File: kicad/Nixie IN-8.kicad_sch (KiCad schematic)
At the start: 47 parts, among them J1 HOURS, J10 DOT, J2 MINUTES, J3 DOT, J4 Conn_01x03_Pin, J5 Conn_01x03_Pin, J6 Conn_01x02_Pin, J7 Barrel_Jack_Switch, J8 HOURS, J9 MINUTES, Q1 MPSA42, SW1 SW_SPST, SW2 SW_SPST, SW3 SW_SPST, U1 K155ID1, U2 K155ID1, U3 K155ID1, U4 K155ID1, U5 MCP7940N-xP, U6 74HC595, U7 74HC595, Y1 32.768kHz

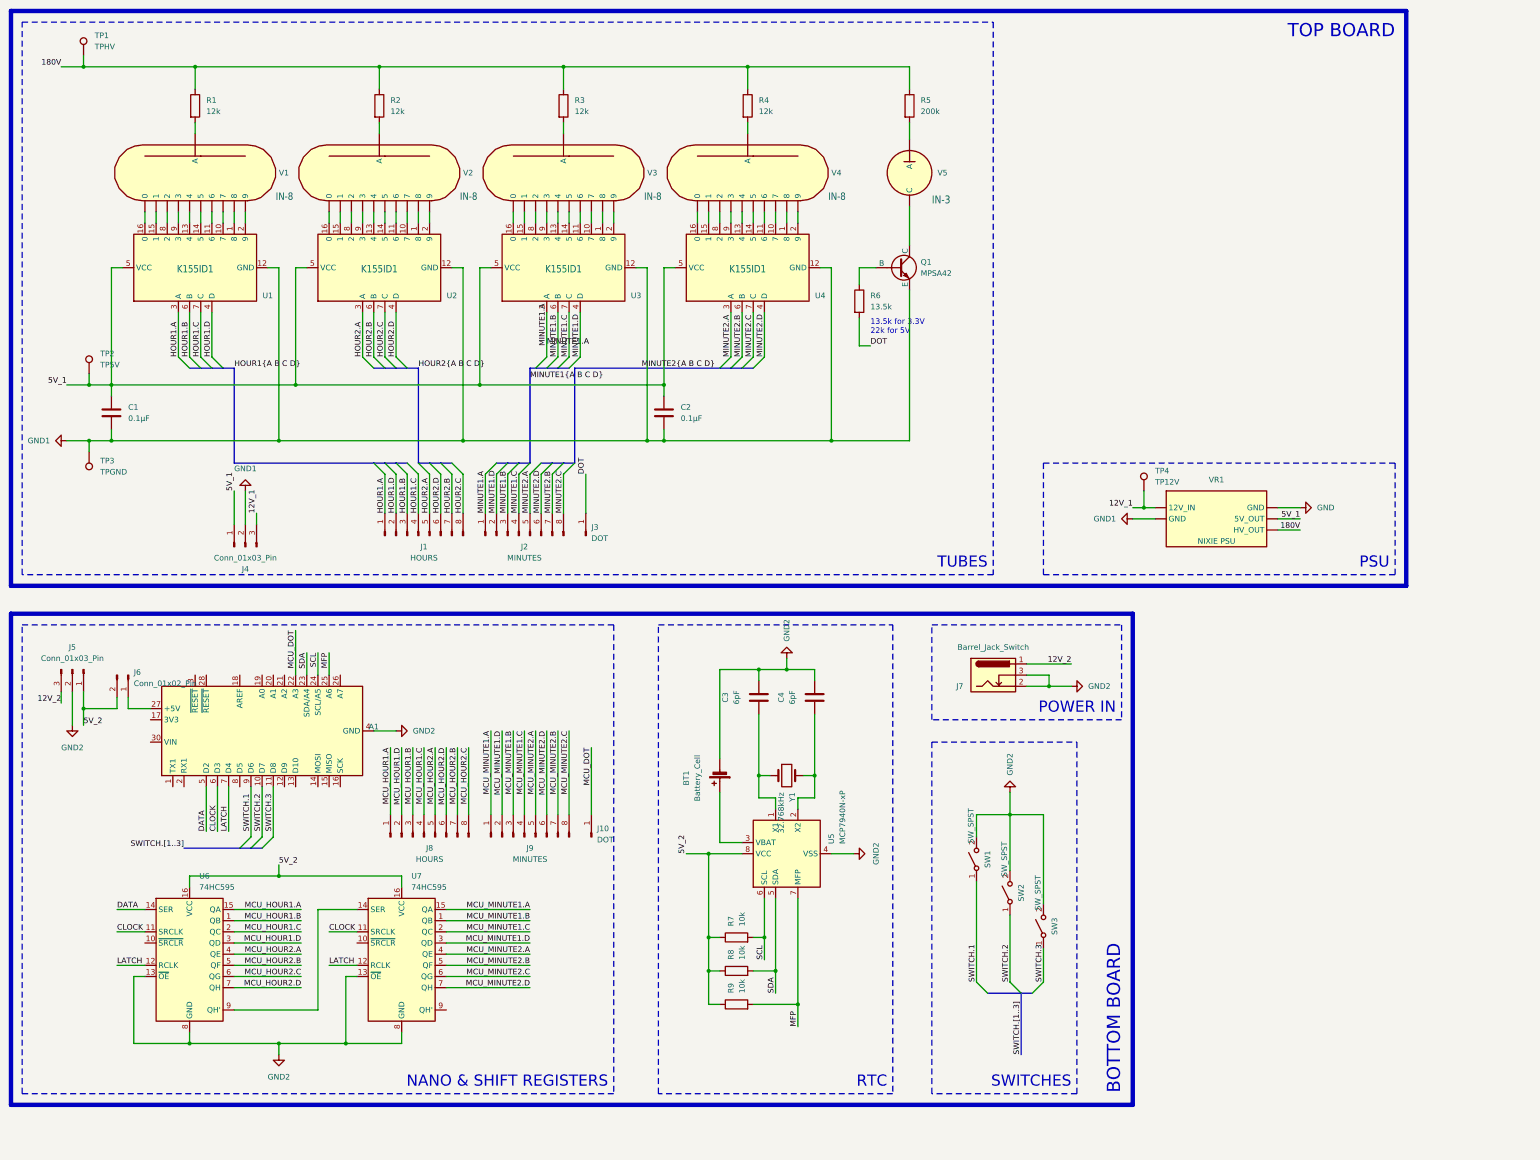
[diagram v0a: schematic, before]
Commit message: removed backups
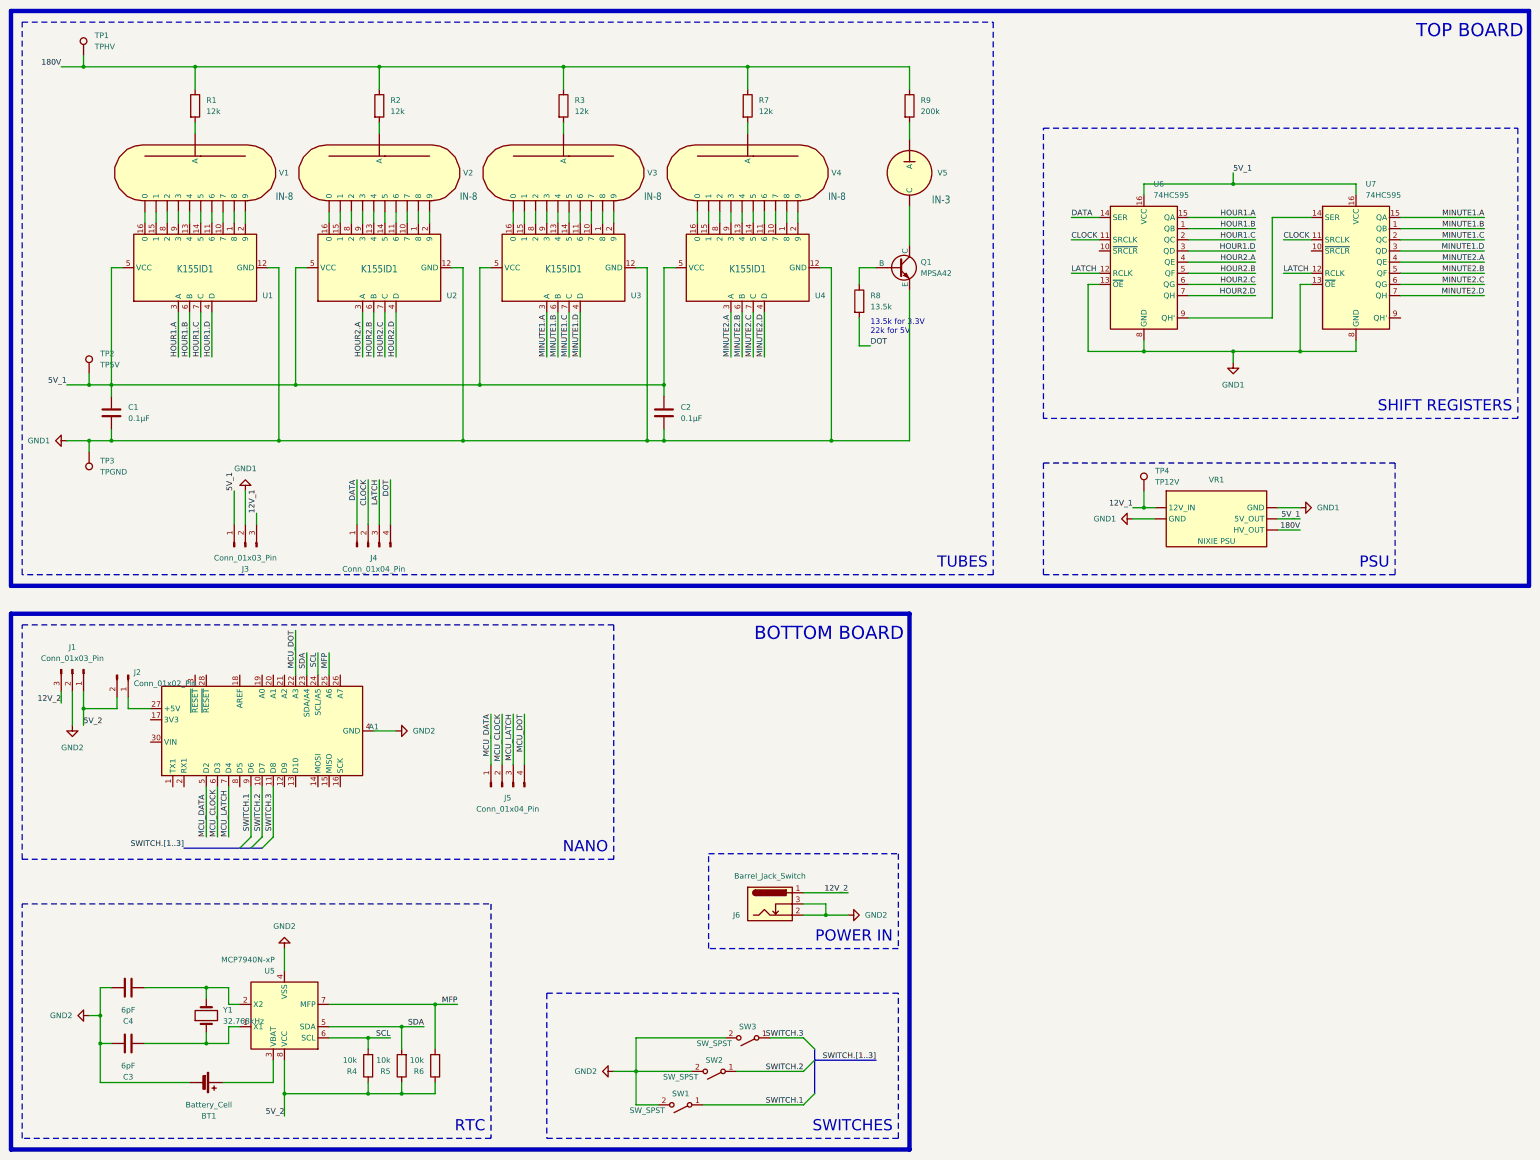
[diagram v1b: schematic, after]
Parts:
- removed J1, J8: HOURS, Connector_PinHeader_2.54mm:PinHeader_1x08_P2.54mm_Vertical, symbol Connector:Conn_01x08_Pin
- removed J10, J3: DOT, Connector_PinHeader_2.54mm:PinHeader_1x01_P2.54mm_Vertical, symbol Connector:Conn_01x01_Pin
- removed J2, J9: MINUTES, Connector_PinHeader_2.54mm:PinHeader_1x08_P2.54mm_Vertical, symbol Connector:Conn_01x08_Pin
- added J4, J5: Conn_01x04_Pin, Connector_PinHeader_2.54mm:PinHeader_1x04_P2.54mm_Vertical, symbol Connector:Conn_01x04_Pin
- renumbered J5 to J1, J6 to J2, J4 to J3, J7 to J6, R7 to R4, R8 to R5, R9 to R6, R4 to R7, R6 to R8, R5 to R9
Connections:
- net GND is gone; now on net GND1: VR1.4 (GND)
- net MCU_HOUR1.A is gone; now on net HOUR1.A: U6.15 (QA)
- net MCU_HOUR1.B is gone; now on net HOUR1.B: U6.1 (QB)
- net MCU_HOUR1.C is gone; now on net HOUR1.C: U6.2 (QC)
- net MCU_HOUR1.D is gone; now on net HOUR1.D: U6.3 (QD)
- net MCU_HOUR2.A is gone; now on net HOUR2.A: U6.4 (QE)
- net MCU_HOUR2.B is gone; now on net HOUR2.B: U6.5 (QF)
- net MCU_HOUR2.C is gone; now on net HOUR2.C: U6.6 (QG)
- net MCU_HOUR2.D is gone; now on net HOUR2.D: U6.7 (QH)
- net MCU_MINUTE1.A is gone; now on net MINUTE1.A: U7.15 (QA)
- net MCU_MINUTE1.B is gone; now on net MINUTE1.B: U7.1 (QB)
- net MCU_MINUTE1.C is gone; now on net MINUTE1.C: U7.2 (QC)
- net MCU_MINUTE1.D is gone; now on net MINUTE1.D: U7.3 (QD)
- net MCU_MINUTE2.A is gone; now on net MINUTE2.A: U7.4 (QE)
- net MCU_MINUTE2.B is gone; now on net MINUTE2.B: U7.5 (QF)
- net MCU_MINUTE2.C is gone; now on net MINUTE2.C: U7.6 (QG)
- net MCU_MINUTE2.D is gone; now on net MINUTE2.D: U7.7 (QH)
- net 5V_1: now also U6.16 (VCC), U7.16 (VCC)
- net 5V_2: no longer U6.16 (VCC), U7.16 (VCC)
- net CLOCK: now also J4.2 (Pin_2); no longer A1.6 (D3)
- net DATA: now also J4.1 (Pin_1); no longer A1.5 (D2)
- net DOT: now also J4.4 (Pin_4)
- net GND1: now also U6.13 (~{OE}), U6.8 (GND), U7.13 (~{OE}), U7.8 (GND)
- net GND2: no longer U6.13 (~{OE}), U6.8 (GND), U7.13 (~{OE}), U7.8 (GND)
- net LATCH: now also J4.3 (Pin_3); no longer A1.7 (D4)
- net MCU_DOT: now also J5.4 (Pin_4)
- new net MCU_CLOCK: A1.6 (D3), J5.2 (Pin_2)
- new net MCU_DATA: A1.5 (D2), J5.1 (Pin_1)
- new net MCU_LATCH: A1.7 (D4), J5.3 (Pin_3)
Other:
- note added: "NANO"
- note added: "SHIFT REGISTERS"
- note removed: "NANO & SHIFT REGISTERS"
- moved on the sheet: BT1, C3, C4, J6, R4, R5, R6, SW1, SW2, SW3, U5, U6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

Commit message: updated pcb
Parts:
- A1: value Arduino_Nano_Every -> ARDUINO NANO EVERY
- BT1: value Battery_Cell -> CR2032
- R8: value 13.5k -> 22k
- TP1: value TPHV -> 180V
- TP2: value TP5V -> 5V
- TP3: value TPGND -> GND
- TP4: value TP12V -> 12V
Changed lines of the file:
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@@
       (effects (font (size 1.27 1.27)) (justify right))
     )
-    (property "Value" "TPGND" (at 44.45 125.222 0)
+    (property "Value" "GND" (at 44.45 125.222 0)
       (effects (font (size 1.27 1.27)) (justify right))
     )
@@
       (effects (font (size 1.27 1.27)) (justify left))
     )
-    (property "Value" "TPHV" (at 43.18 28.448 0)
+    (property "Value" "180V" (at 43.18 28.448 0)
       (effects (font (size 1.27 1.27)) (justify left))
     )
@@
   )
   (symbol (lib_id "Device:Battery_Cell") (at 67.31 264.16 270) (unit 1)
-    (in_bom yes) (on_board yes) (dnp no) (fields_autoplaced)
-    (property "Reference" "BT1" (at 69.1515 271.78 90)
-      (effects (font (size 1.27 1.27)))
-    )
-    (property "Value" "Battery_Cell" (at 69.1515 269.24 90)
+    (in_bom yes) (on_board yes) (dnp no)
+    (property "Reference" "BT1" (at 68.58 267.97 90)
+      (effects (font (size 1.27 1.27)))
+    )
+    (property "Value" "CR2032" (at 68.58 270.51 90)
       (effects (font (size 1.27 1.27)))
     )
@@
       (effects (font (size 1.27 1.27)) (justify left))
     )
-    (property "Value" "TP5V" (at 44.45 100.838 0)
+    (property "Value" "5V" (at 44.45 100.838 0)
       (effects (font (size 1.27 1.27)) (justify left))
     )
@@
       (effects (font (size 1.27 1.27)) (justify left))
     )
-    (property "Value" "13.5k" (at 219.71 87.63 0)
+    (property "Value" "22k" (at 219.71 87.63 0)
       (effects (font (size 1.27 1.27)) (justify left))
     )
@@
       (effects (font (size 1.27 1.27)))
     )
-    (property "Value" "Arduino_Nano_Every" (at 109.22 181.9559 0)
+    (property "Value" "ARDUINO NANO EVERY" (at 109.22 181.9559 0)
       (effects (font (size 1.27 1.27)) (justify left) hide)
     )
@@
       (effects (font (size 1.27 1.27)) (justify left))
     )
-    (property "Value" "TP12V" (at 284.48 127.508 0)
-      (effects (font (size 1.27 1.27)) (justify left))
-    )
+    (property "Value" "12V" (at 284.48 127.508 0)
+      (effects (font (size 1.27 1.27)) (justify left))
+    )

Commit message: setup board
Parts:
- removed TP2: 5V, TestPoint:TestPoint_THTPad_D2.5mm_Drill1.2mm, symbol Connector:TestPoint
- removed U1, U2, U3, U4: K155ID1, Package_DIP:DIP-16_W7.62mm_Socket, symbol Nixie:K155D1
- added C3, C4, C5: 0.1µF, Capacitor_THT:C_Disc_D3.0mm_W1.6mm_P2.50mm, symbol Device:C
- added Q1, Q10, Q11, Q12, Q13, Q14, Q15, Q16, Q17, Q18, Q19, Q2, Q20, Q21, Q22, Q23, Q24, Q25, Q26, Q27, Q28, Q29, Q3, Q30, Q31, Q32, Q33, Q34, Q35, Q36, Q37, Q38, Q39, Q4, Q40, Q41, Q6, Q7, Q8, Q9: MPSA42, Package_TO_SOT_THT:TO-92_Inline_Wide, symbol Nixie:NPN-MPSA42
- added R6, R7, R8, R9: 22k, Resistor_THT:R_Axial_DIN0204_L3.6mm_D1.6mm_P5.08mm_Vertical, symbol Device:R
- added TP4: GND, TestPoint:TestPoint_THTPad_D2.5mm_Drill1.2mm, symbol Connector:TestPoint
- added U3, U4, U5: 74HC595, Package_SO:SOIC-16_3.9x9.9mm_P1.27mm, symbol 74xx:74HC595
- TP3: value GND -> 5V
- renumbered C4 to C6, C3 to C7, J3 to J1, J4 to J2, J1 to J3, J5 to J4, J2 to J5, Q1 to Q5, R8 to R10, R4 to R11, R5 to R12, R6 to R13, R7 to R4, R9 to R5, SW3 to SW1, SW1 to SW3, TP4 to TP2, U6 to U1, U7 to U2, U5 to U6
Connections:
- net 5V_1: now also TP3.1, C3.1, C4.1, C5.1, R6.2, R7.2, R8.2, R9.2, U3.16 (VCC), U4.16 (VCC), U5.16 (VCC)
- net CLOCK: now also U3.11 (SRCLK), U4.11 (SRCLK), U5.11 (SRCLK)
- net GND1: now also C3.2, C4.2, C5.2, TP4.1, U3.13 (~{OE}), U3.8 (GND), U4.13 (~{OE}), U4.8 (GND), U5.13 (~{OE}), U5.8 (GND); no longer TP3.1
- net LATCH: now also U3.12 (RCLK), U4.12 (RCLK), U5.12 (RCLK)
- net at U2.9 (QH'): now also U3.14 (SER)
- net at V2.8: now also Q35.3 (C)
- net at V2.7: now also Q31.3 (C)
- net at V2.6: now also Q27.3 (C)
- net at V2.4: now also Q19.3 (C)
- net at V2.5: now also Q23.3 (C)
- net at V2.1: now also Q7.3 (C)
- net at V2.10 (0): now also Q2.3 (C)
- net at V2.9: now also Q39.3 (C)
- net at V2.2: now also Q11.3 (C)
- net at V2.3: now also Q15.3 (C)
- net at V4.1: now also Q9.3 (C)
- net at V4.10 (0): now also Q4.3 (C)
- net at V4.2: now also Q13.3 (C)
- net at V4.3: now also Q17.3 (C)
- net at V4.4: now also Q21.3 (C)
- net at V4.5: now also Q25.3 (C)
- net at V4.6: now also Q29.3 (C)
- net at V4.7: now also Q33.3 (C)
- net at V4.8: now also Q37.3 (C)
- net at V4.9: now also Q41.3 (C)
- net at V3.1: now also Q8.3 (C)
- net at V3.10 (0): now also Q3.3 (C)
- net at V3.2: now also Q12.3 (C)
- net at V3.3: now also Q16.3 (C)
- net at V3.4: now also Q20.3 (C)
- net at V3.5: now also Q24.3 (C)
- net at V3.6: now also Q28.3 (C)
- net at V3.7: now also Q32.3 (C)
- net at V3.8: now also Q36.3 (C)
- net at V3.9: now also Q40.3 (C)
- net at V1.1: now also Q6.3 (C)
- net at V1.10 (0): now also Q1.3 (C)
- net at V1.2: now also Q10.3 (C)
- net at V1.3: now also Q14.3 (C)
- net at V1.4: now also Q18.3 (C)
- net at V1.5: now also Q22.3 (C)
- net at V1.6: now also Q26.3 (C)
- net at V1.7: now also Q30.3 (C)
- net at V1.8: now also Q34.3 (C)
- net at V1.9: now also Q38.3 (C)
- net HOUR1.A renamed HOUR1.0
- net HOUR1.0: now also Q1.1 (E)
- net HOUR1.B renamed HOUR1.1
- net HOUR1.1: now also Q6.1 (E)
- net HOUR1.C renamed HOUR1.2
- net HOUR1.2: now also Q10.1 (E)
- net HOUR1.D renamed HOUR1.3
- net HOUR1.3: now also Q14.1 (E)
- net HOUR2.A renamed HOUR1.4
- net HOUR1.4: now also Q18.1 (E)
- net HOUR2.B renamed HOUR1.5
- net HOUR1.5: now also Q22.1 (E)
- net HOUR2.C renamed HOUR1.6
- net HOUR1.6: now also Q26.1 (E)
- net HOUR2.D renamed HOUR1.7
- net HOUR1.7: now also Q30.1 (E)
- net MINUTE1.A renamed HOUR1.8
- net HOUR1.8: now also Q34.1 (E)
- net MINUTE1.B renamed HOUR1.9
- net HOUR1.9: now also Q38.1 (E)
- net MINUTE1.C renamed HOUR2.0
- net HOUR2.0: now also Q2.1 (E)
- net MINUTE1.D renamed HOUR2.1
- net HOUR2.1: now also Q7.1 (E)
- net MINUTE2.A renamed HOUR2.2
- net HOUR2.2: now also Q11.1 (E)
- net MINUTE2.B renamed HOUR2.3
- net HOUR2.3: now also Q15.1 (E)
- net MINUTE2.C renamed HOUR2.4
- net HOUR2.4: now also Q19.1 (E)
- net MINUTE2.D renamed HOUR2.5
- net HOUR2.5: now also Q23.1 (E)
- new net: U4.9 (QH'), U5.14 (SER)
- new net: Q1.2 (B), Q10.2 (B), Q14.2 (B), Q18.2 (B), Q22.2 (B), Q26.2 (B), Q30.2 (B), Q34.2 (B), Q38.2 (B), Q6.2 (B), R6.1
- new net: Q11.2 (B), Q15.2 (B), Q19.2 (B), Q2.2 (B), Q23.2 (B), Q27.2 (B), Q31.2 (B), Q35.2 (B), Q39.2 (B), Q7.2 (B), R7.1
- new net: Q12.2 (B), Q16.2 (B), Q20.2 (B), Q24.2 (B), Q28.2 (B), Q3.2 (B), Q32.2 (B), Q36.2 (B), Q40.2 (B), Q8.2 (B), R8.1
- new net: Q13.2 (B), Q17.2 (B), Q21.2 (B), Q25.2 (B), Q29.2 (B), Q33.2 (B), Q37.2 (B), Q4.2 (B), Q41.2 (B), Q9.2 (B), R9.1
- new net: U3.9 (QH'), U4.14 (SER)
- new net HOUR2.6: Q27.1 (E), U3.15 (QA)
- new net HOUR2.7: Q31.1 (E), U3.1 (QB)
- new net HOUR2.8: Q35.1 (E), U3.2 (QC)
- new net HOUR2.9: Q39.1 (E), U3.3 (QD)
- new net MINUTE1.0: Q3.1 (E), U3.4 (QE)
- new net MINUTE1.1: Q8.1 (E), U3.5 (QF)
- new net MINUTE1.2: Q12.1 (E), U3.6 (QG)
- new net MINUTE1.3: Q16.1 (E), U3.7 (QH)
- new net MINUTE1.4: Q20.1 (E), U4.15 (QA)
- new net MINUTE1.5: Q24.1 (E), U4.1 (QB)
- new net MINUTE1.6: Q28.1 (E), U4.2 (QC)
- new net MINUTE1.7: Q32.1 (E), U4.3 (QD)
- new net MINUTE1.8: Q36.1 (E), U4.4 (QE)
- new net MINUTE1.9: Q40.1 (E), U4.5 (QF)
- new net MINUTE2.0: Q4.1 (E), U4.6 (QG)
- new net MINUTE2.1: Q9.1 (E), U4.7 (QH)
- new net MINUTE2.2: Q13.1 (E), U5.15 (QA)
- new net MINUTE2.3: Q17.1 (E), U5.1 (QB)
- new net MINUTE2.4: Q21.1 (E), U5.2 (QC)
- new net MINUTE2.5: Q25.1 (E), U5.3 (QD)
- new net MINUTE2.6: Q29.1 (E), U5.4 (QE)
- new net MINUTE2.7: Q33.1 (E), U5.5 (QF)
- new net MINUTE2.8: Q37.1 (E), U5.6 (QG)
- new net MINUTE2.9: Q41.1 (E), U5.7 (QH)
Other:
- note added: "MCU"
- note removed: "NANO"
- note removed: "POWER IN"
- note removed: "PSU"
- moved on the sheet: A1, BT1, C6, C7, J1, J2, J3, J4, J5, J6, Q5, R1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

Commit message: finished routing
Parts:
- removed A1: ARDUINO NANO EVERY, Nixie:Arduino_Nano_SMT, symbol MCU_Module:Arduino_Nano_Every
- removed J5: Conn_01x02_Pin, Connector_PinHeader_2.54mm:PinHeader_1x02_P2.54mm_Horizontal, symbol Connector:Conn_01x02_Pin
- added D1: D, Diode_SMD:D_SMA_Handsoldering, symbol Device:D
- added J3, J7: Conn_01x04_Pin, Connector_PinHeader_2.54mm:PinHeader_1x04_P2.54mm_Vertical, symbol Connector:Conn_01x04_Pin
- added J4, J8: Conn_01x02_Pin, Connector_PinHeader_2.54mm:PinHeader_1x02_P2.54mm_Vertical, symbol Connector:Conn_01x02_Pin
- added U7: Pico, MCU_RaspberryPi_and_Boards:RPi_Pico_SMD, symbol MCU_RaspberryPi_and_Boards:Pico
- R10, R6, R7, R8, R9: value 22k -> 13.5k
- renumbered J3 to J5, J4 to J6, J6 to J9
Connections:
- net 5V_1: no longer C1.1, C2.1, C3.1, C4.1, C5.1, R6.2, R7.2, R8.2, R9.2, U1.16 (VCC), U2.16 (VCC), U3.16 (VCC), U4.16 (VCC), U5.16 (VCC)
- net 5V_2: now also D1.2 (A); no longer R11.1, R12.1, R13.1, U6.8 (VCC)
- net GND1: no longer U1.13 (~{OE}), U2.13 (~{OE}), U3.13 (~{OE}), U4.13 (~{OE}), U5.13 (~{OE})
- net GND2: now also U7.38 (GND)
- net MCU_CLOCK: now also U7.11 (GPIO8)
- net MCU_DATA: now also U7.12 (GPIO9)
- net MCU_DOT: now also U7.9 (GPIO6)
- net MCU_LATCH: now also U7.10 (GPIO7)
- net MFP: now also U7.25 (GPIO19)
- net SCL: now also U7.26 (GPIO20)
- net SDA: now also U7.27 (GPIO21)
- net SWITCH.1: now also U7.31 (GPIO26_ADC0)
- net SWITCH.2: now also U7.32 (GPIO27_ADC1)
- net SWITCH.3: now also U7.34 (GPIO28_ADC2)
- new net: D1.1 (K), U7.39 (VSYS)
- new net 3.3V_1: C1.1, C2.1, C3.1, C4.1, C5.1, J4.1 (Pin_1), U1.16 (VCC), U2.16 (VCC), U3.16 (VCC), U4.16 (VCC), U5.16 (VCC)
- new net 3.3V_2: J8.1 (Pin_1), R11.1, R12.1, R13.1, U6.8 (VCC), U7.36 (3V3)
- new net HOUR1_EN: J3.1 (Pin_1), R6.2
- new net HOUR2_EN: J3.2 (Pin_2), R7.2
- new net MCU_HOUR1_EN: J7.1 (Pin_1), U7.17 (GPIO13)
- new net MCU_HOUR2_EN: J7.2 (Pin_2), U7.16 (GPIO12)
- new net MCU_MINUTE1_EN: J7.3 (Pin_3), U7.15 (GPIO11)
- new net MCU_MINUTE2_EN: J7.4 (Pin_4), U7.14 (GPIO10)
- new net MCU_OE: J8.2 (Pin_2), U7.19 (GPIO14)
- new net MINUTE1_EN: J3.3 (Pin_3), R8.2
- new net MINUTE2_EN: J3.4 (Pin_4), R9.2
- new net OE: J4.2 (Pin_2), U1.13 (~{OE}), U2.13 (~{OE}), U3.13 (~{OE}), U4.13 (~{OE}), U5.13 (~{OE})
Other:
- moved on the sheet: J6, J9
